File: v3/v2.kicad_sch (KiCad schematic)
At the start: 112 parts, among them J2 Conn_01x04_Pin, J3 Conn_01x04_Pin, SW1 SW_Push, SW10 SW_Push, SW11 SW_Push, SW12 SW_Push, SW13 SW_Push, SW14 SW_Push, SW15 SW_Push, SW16 SW_Push, SW17 SW_Push, SW18 SW_Push, SW19 SW_Push, SW2 SW_Push, SW20 SW_Push, SW21 SW_Push, SW22 SW_Push, SW23 SW_Push, SW24 SW_Push, SW25 SW_Push, SW26 SW_Push, SW27 SW_Push, SW28 SW_Push, SW29 SW_Push, SW3 SW_Push, SW30 SW_Push, SW31 SW_Push, SW32 SW_Push, SW33 RotaryEncoder_Switch, SW4 SW_Push, SW5 SW_Push, SW6 SW_Push, SW7 SW_Push, SW8 SW_Push, SW9 SW_Push, U1 Pico, U2 Pico

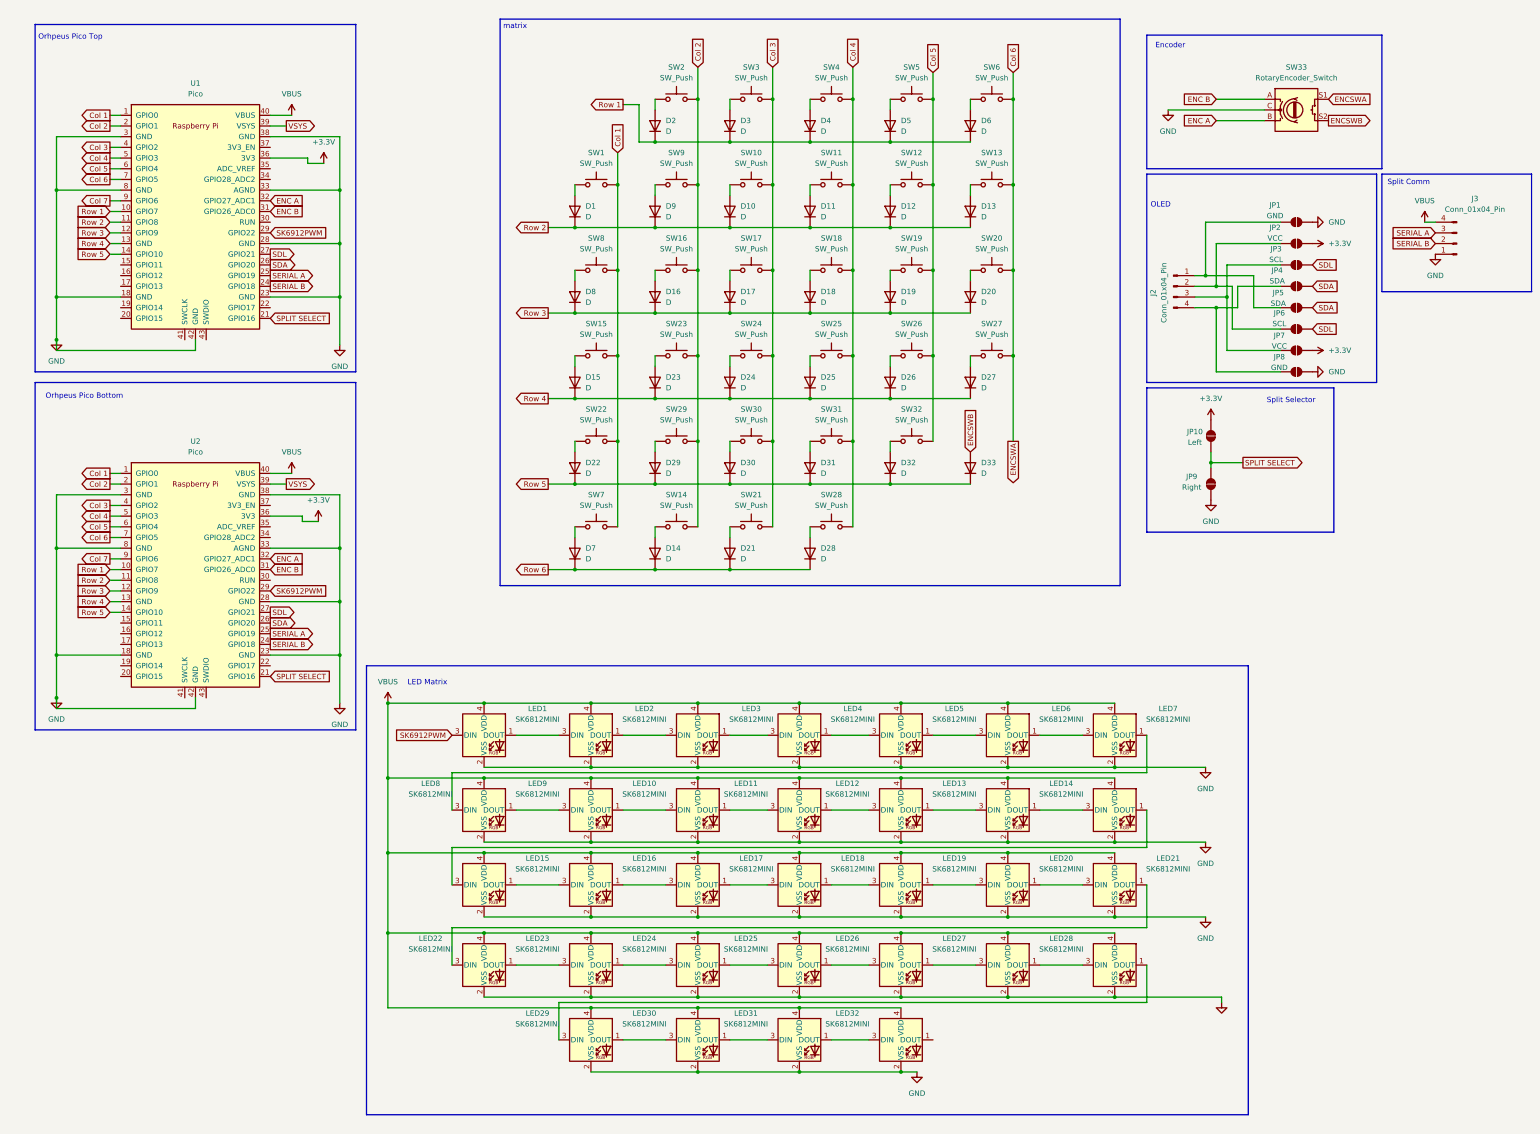
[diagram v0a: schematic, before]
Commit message: redid footprints and layout for pcb
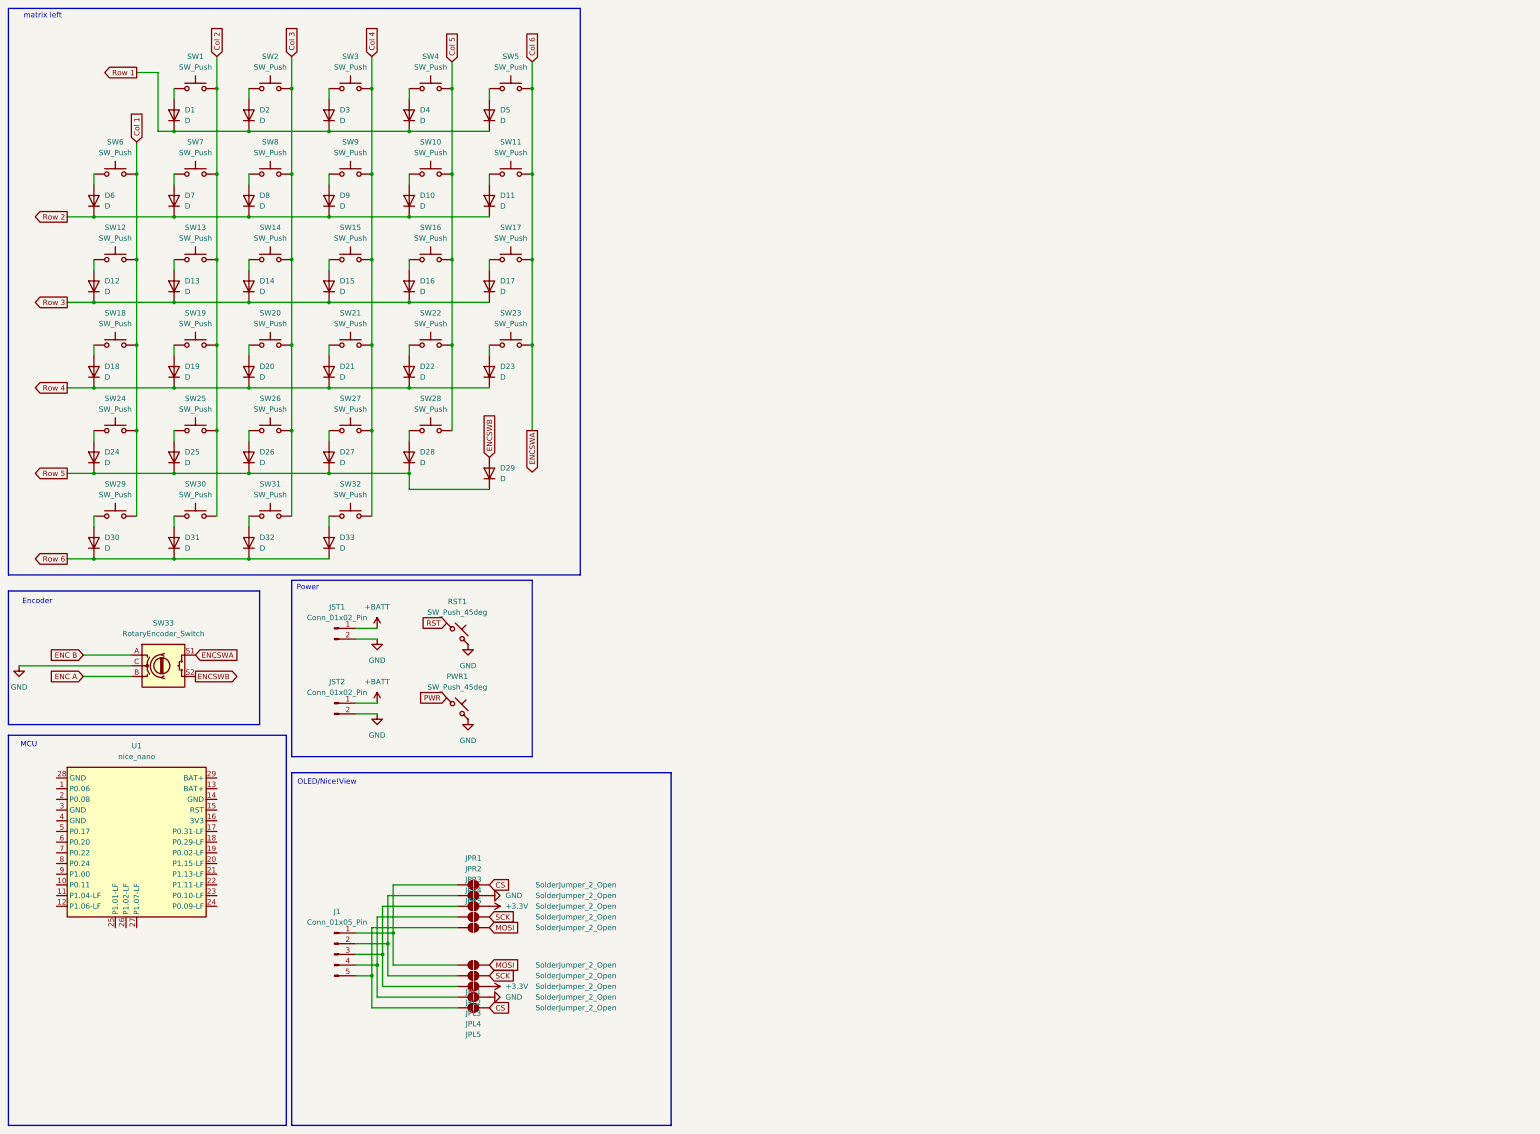
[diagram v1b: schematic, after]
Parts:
- removed J2: Conn_01x04_Pin, Keebio-Parts:I2C_Breakout, symbol Connector:Conn_01x04_Pin
- removed J3: Conn_01x04_Pin, Keebio-Parts:TRRS-PJ-320A-dual, symbol Connector:Conn_01x04_Pin
- removed JP1, JP8: GND, Jumper:SolderJumper-2_P1.3mm_Open_RoundedPad1.0x1.5mm, symbol Jumper:SolderJumper_2_Open
- removed JP10: Left, Jumper:SolderJumper-2_P1.3mm_Open_RoundedPad1.0x1.5mm, symbol Jumper:SolderJumper_2_Open
- removed JP2, JP7: VCC, Jumper:SolderJumper-2_P1.3mm_Open_RoundedPad1.0x1.5mm, symbol Jumper:SolderJumper_2_Open
- removed JP3, JP6: SCL, Jumper:SolderJumper-2_P1.3mm_Open_RoundedPad1.0x1.5mm, symbol Jumper:SolderJumper_2_Open
- removed JP4, JP5: SDA, Jumper:SolderJumper-2_P1.3mm_Open_RoundedPad1.0x1.5mm, symbol Jumper:SolderJumper_2_Open
- removed JP9: Right, Jumper:SolderJumper-2_P1.3mm_Open_RoundedPad1.0x1.5mm, symbol Jumper:SolderJumper_2_Open
- removed LED1, LED10, LED11, LED12, LED13, LED14, LED15, LED16, LED17, LED18, LED19, LED2, LED20, LED21, LED22, LED23, LED24, LED25, LED26, LED27, LED28, LED29, LED3, LED30, LED31, LED32, LED4, LED5, LED6, LED7, LED8, LED9: SK6812MINI, reversible-kicad-footprints:MX-1U-SK6812Mini-E, symbol LED:SK6812MINI
- removed U1, U2: Pico, Module:RaspberryPi_Pico_SMD_HandSolder, symbol RPi_Pico:Pico
- added J1: Conn_01x05_Pin, Connector_PinHeader_1.00mm:PinHeader_1x05_P1.00mm_Vertical, symbol Connector:Conn_01x05_Pin
- added JPL1, JPL2, JPL3, JPL4, JPL5, JPR1, JPR2, JPR3, JPR4, JPR5: SolderJumper_2_Open, Jumper:SolderJumper-2_P1.3mm_Open_RoundedPad1.0x1.5mm, symbol Jumper:SolderJumper_2_Open
- added JST1, JST2: Conn_01x02_Pin, Connector_JST:JST_PH_S2B-PH-K_1x02_P2.00mm_Horizontal, symbol Connector:Conn_01x02_Pin
- added PWR1, RST1: SW_Push_45deg, reversible-kicad-footprints:SMD_Push, symbol Switch:SW_Push_45deg
- added U1: nice_nano, PCM_marbastlib-xp-promicroish:nice_nano_AH_USBup, symbol PCM_marbastlib-promicroish:nice_nano
- D1: renamed from D2; footprint Keebio-Parts:Diode-Hybrid-Dual -> footprints:Diode-dual
- D10: renamed from D12; footprint Keebio-Parts:Diode-Hybrid-Dual -> footprints:Diode-dual
- D11: renamed from D13; footprint Keebio-Parts:Diode-Hybrid-Dual -> footprints:Diode-dual
- D12: renamed from D8; footprint Keebio-Parts:Diode-Hybrid-Dual -> footprints:Diode-dual
- D13: renamed from D16; footprint Keebio-Parts:Diode-Hybrid-Dual -> footprints:Diode-dual
- D14: renamed from D17; footprint Keebio-Parts:Diode-Hybrid-Dual -> footprints:Diode-dual
- D15: renamed from D18; footprint Keebio-Parts:Diode-Hybrid-Dual -> footprints:Diode-dual
- D16: renamed from D19; footprint Keebio-Parts:Diode-Hybrid-Dual -> footprints:Diode-dual
- D17: renamed from D20; footprint Keebio-Parts:Diode-Hybrid-Dual -> footprints:Diode-dual
- D18: renamed from D15; footprint Keebio-Parts:Diode-Hybrid-Dual -> footprints:Diode-dual
- D19: renamed from D23; footprint Keebio-Parts:Diode-Hybrid-Dual -> footprints:Diode-dual
- D2: renamed from D3; footprint Keebio-Parts:Diode-Hybrid-Dual -> footprints:Diode-dual
- D20: renamed from D24; footprint Keebio-Parts:Diode-Hybrid-Dual -> footprints:Diode-dual
- D21: renamed from D25; footprint Keebio-Parts:Diode-Hybrid-Dual -> footprints:Diode-dual
- D22: renamed from D26; footprint Keebio-Parts:Diode-Hybrid-Dual -> footprints:Diode-dual
- D23: renamed from D27; footprint Keebio-Parts:Diode-Hybrid-Dual -> footprints:Diode-dual
- D24: renamed from D22; footprint Keebio-Parts:Diode-Hybrid-Dual -> footprints:Diode-dual
- D25: renamed from D29; footprint Keebio-Parts:Diode-Hybrid-Dual -> footprints:Diode-dual
- D26: renamed from D30; footprint Keebio-Parts:Diode-Hybrid-Dual -> footprints:Diode-dual
- D27: renamed from D31; footprint Keebio-Parts:Diode-Hybrid-Dual -> footprints:Diode-dual
- D28: renamed from D32; footprint Keebio-Parts:Diode-Hybrid-Dual -> footprints:Diode-dual
- D29: renamed from D33; footprint Keebio-Parts:Diode-Hybrid-Dual -> footprints:Diode-dual
- D3: renamed from D4; footprint Keebio-Parts:Diode-Hybrid-Dual -> footprints:Diode-dual
- D30: renamed from D7; footprint Keebio-Parts:Diode-Hybrid-Dual -> footprints:Diode-dual
- D31: renamed from D14; footprint Keebio-Parts:Diode-Hybrid-Dual -> footprints:Diode-dual
- D32: renamed from D21; footprint Keebio-Parts:Diode-Hybrid-Dual -> footprints:Diode-dual
- D33: renamed from D28; footprint Keebio-Parts:Diode-Hybrid-Dual -> footprints:Diode-dual
- D4: renamed from D5; footprint Keebio-Parts:Diode-Hybrid-Dual -> footprints:Diode-dual
- D5: renamed from D6; footprint Keebio-Parts:Diode-Hybrid-Dual -> footprints:Diode-dual
- D6: renamed from D1; footprint Keebio-Parts:Diode-Hybrid-Dual -> footprints:Diode-dual
- D7: renamed from D9; footprint Keebio-Parts:Diode-Hybrid-Dual -> footprints:Diode-dual
- D8: renamed from D10; footprint Keebio-Parts:Diode-Hybrid-Dual -> footprints:Diode-dual
- D9: renamed from D11; footprint Keebio-Parts:Diode-Hybrid-Dual -> footprints:Diode-dual
- SW1: renamed from SW2; footprint reversible-kicad-footprints:MX-1U-Hotswap -> footprints:gateron-ks27-hotswap-reversible
- SW10: renamed from SW12; footprint reversible-kicad-footprints:MX-1U-Hotswap -> footprints:gateron-ks27-hotswap-reversible
- SW11: renamed from SW13; footprint reversible-kicad-footprints:MX-1U-Hotswap -> footprints:gateron-ks27-hotswap-reversible
- SW12: renamed from SW8; footprint reversible-kicad-footprints:MX-1U-Hotswap -> footprints:gateron-ks27-hotswap-reversible
- SW13: renamed from SW16; footprint reversible-kicad-footprints:MX-1U-Hotswap -> footprints:gateron-ks27-hotswap-reversible
- SW14: renamed from SW17; footprint reversible-kicad-footprints:MX-1U-Hotswap -> footprints:gateron-ks27-hotswap-reversible
- SW15: renamed from SW18; footprint reversible-kicad-footprints:MX-1U-Hotswap -> footprints:gateron-ks27-hotswap-reversible
- SW16: renamed from SW19; footprint reversible-kicad-footprints:MX-1U-Hotswap -> footprints:gateron-ks27-hotswap-reversible
- SW17: renamed from SW20; footprint reversible-kicad-footprints:MX-1U-Hotswap -> footprints:gateron-ks27-hotswap-reversible
- SW18: renamed from SW15; footprint reversible-kicad-footprints:MX-1U-Hotswap -> footprints:gateron-ks27-hotswap-reversible
- SW19: renamed from SW23; footprint reversible-kicad-footprints:MX-1U-Hotswap -> footprints:gateron-ks27-hotswap-reversible
- SW2: renamed from SW3; footprint reversible-kicad-footprints:MX-1U-Hotswap -> footprints:gateron-ks27-hotswap-reversible
- SW20: renamed from SW24; footprint reversible-kicad-footprints:MX-1U-Hotswap -> footprints:gateron-ks27-hotswap-reversible
- SW21: renamed from SW25; footprint reversible-kicad-footprints:MX-1U-Hotswap -> footprints:gateron-ks27-hotswap-reversible
- SW22: renamed from SW26; footprint reversible-kicad-footprints:MX-1U-Hotswap -> footprints:gateron-ks27-hotswap-reversible
- SW23: renamed from SW27; footprint reversible-kicad-footprints:MX-1U-Hotswap -> footprints:gateron-ks27-hotswap-reversible
- SW24: renamed from SW22; footprint reversible-kicad-footprints:MX-1U-Hotswap -> footprints:gateron-ks27-hotswap-reversible
- SW25: renamed from SW29; footprint reversible-kicad-footprints:MX-1U-Hotswap -> footprints:gateron-ks27-hotswap-reversible
- SW26: renamed from SW30; footprint reversible-kicad-footprints:MX-1U-Hotswap -> footprints:gateron-ks27-hotswap-reversible
- SW27: renamed from SW31; footprint reversible-kicad-footprints:MX-1U-Hotswap -> footprints:gateron-ks27-hotswap-reversible
- SW28: renamed from SW32; footprint reversible-kicad-footprints:MX-1U-Hotswap -> footprints:gateron-ks27-hotswap-reversible
- SW29: renamed from SW7; footprint reversible-kicad-footprints:MX-1U-Hotswap -> footprints:gateron-ks27-hotswap-reversible
- SW3: renamed from SW4; footprint reversible-kicad-footprints:MX-1U-Hotswap -> footprints:gateron-ks27-hotswap-reversible
- SW30: renamed from SW14; footprint reversible-kicad-footprints:MX-1U-Hotswap -> footprints:gateron-ks27-hotswap-reversible
- SW31: renamed from SW21; footprint reversible-kicad-footprints:MX-1U-Hotswap -> footprints:gateron-ks27-hotswap-reversible
- SW32: renamed from SW28; footprint reversible-kicad-footprints:MX-1U-Hotswap -> footprints:gateron-ks27-hotswap-reversible
- SW33: footprint Keebio-Parts:RotaryEncoder_EC11 -> Keebio-Parts.pretty-master:RotaryEncoder_EC11
- SW4: renamed from SW5; footprint reversible-kicad-footprints:MX-1U-Hotswap -> footprints:gateron-ks27-hotswap-reversible
- SW5: renamed from SW6; footprint reversible-kicad-footprints:MX-1U-Hotswap -> footprints:gateron-ks27-hotswap-reversible
- SW6: renamed from SW1; footprint reversible-kicad-footprints:MX-1U-Hotswap -> footprints:gateron-ks27-hotswap-reversible
- SW7: renamed from SW9; footprint reversible-kicad-footprints:MX-1U-Hotswap -> footprints:gateron-ks27-hotswap-reversible
- SW8: renamed from SW10; footprint reversible-kicad-footprints:MX-1U-Hotswap -> footprints:gateron-ks27-hotswap-reversible
- SW9: renamed from SW11; footprint reversible-kicad-footprints:MX-1U-Hotswap -> footprints:gateron-ks27-hotswap-reversible
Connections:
- net +3.3V: now also JPL3.2 (B), JPR3.2 (B)
- net GND: now also JPL4.2 (B), JPR2.2 (B), JST1.2 (Pin_2), JST2.2 (Pin_2), PWR1.2, RST1.2
- new net: J1.5 (Pin_5), JPL5.1 (A), JPR5.1 (A)
- new net: J1.1 (Pin_1), JPL1.1 (A), JPR1.1 (A)
- new net: J1.2 (Pin_2), JPL2.1 (A), JPR2.1 (A)
- new net: J1.3 (Pin_3), JPL3.1 (A), JPR3.1 (A)
- new net: J1.4 (Pin_4), JPL4.1 (A), JPR4.1 (A)
- new net +BATT: JST1.1 (Pin_1), JST2.1 (Pin_1)
- new net CS: JPL5.2 (B), JPR1.2 (B)
- new net MOSI: JPL1.2 (B), JPR5.2 (B)
- new net PWR: PWR1.1
- new net RST: RST1.1
- new net SCK: JPL2.2 (B), JPR4.2 (B)
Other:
- note added: "MCU"
- note added: "OLED/Nice!View"
- note added: "Power"
- note added: "matrix left"
- note removed: "LED Matrix"
- note removed: "OLED"
- note removed: "Orhpeus Pico Bottom"
- note removed: "Orhpeus Pico Top"
- note removed: "Split Comm"
- note removed: "Split Selector"
- note removed: "matrix"
- moved on the sheet: D1, D10, D11, D12, D13, D14, D15, D16, D17, D18, D19, D2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

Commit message: start placing switches
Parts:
- J1: footprint Connector_PinHeader_1.00mm:PinHeader_1x05_P1.00mm_Vertical -> Connector_PinHeader_2.54mm:PinHeader_1x05_P2.54mm_Vertical
- PWR1, RST1: footprint reversible-kicad-footprints:SMD_Push -> footprints:EVQ-P7C-Reversible
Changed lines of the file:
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@@
 			)
 		)
-		(property "Footprint" "Connector_PinHeader_1.00mm:PinHeader_1x05_P1.00mm_Vertical"
+		(property "Footprint" "Connector_PinHeader_2.54mm:PinHeader_1x05_P2.54mm_Vertical"
 			(at 95.25 241.3 0)
 			(effects
@@
 			)
 		)
-		(property "Footprint" "reversible-kicad-footprints:SMD_Push"
+		(property "Footprint" "footprints:EVQ-P7C-Reversible"
 			(at 124.46 165.1 0)
 			(effects
@@
 			)
 		)
-		(property "Footprint" "reversible-kicad-footprints:SMD_Push"
+		(property "Footprint" "footprints:EVQ-P7C-Reversible"
 			(at 124.46 182.88 0)
 			(effects

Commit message: added all needed labels
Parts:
- added U2: nice_nano_right, PCM_marbastlib-xp-promicroish:nice_nano_AH_USBup, symbol PCM_marbastlib-promicroish:nice_nano
- U1: value nice_nano -> nice_nano_left
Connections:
- net +3.3V: now also U1.16 (3V3), U2.16 (3V3)
- net +BATT: now also U1.13 (BAT+), U1.29 (BAT+), U2.13 (BAT+), U2.29 (BAT+)
- net CS: now also U1.1 (P0.06), U2.1 (P0.06)
- net Col 1: now also U1.2 (P0.08), U2.2 (P0.08)
- net Col 2: now also U1.7 (P0.22), U2.7 (P0.22)
- net Col 3: now also U1.8 (P0.24), U2.8 (P0.24)
- net Col 4: now also U1.9 (P1.00), U2.9 (P1.00)
- net Col 5: now also U1.10 (P0.11), U2.10 (P0.11)
- net Col 6: now also U1.11 (P1.04-LF), U2.11 (P1.04-LF)
- net ENC A: now also U1.12 (P1.06-LF), U2.12 (P1.06-LF)
- net ENC B: now also U1.23 (P0.10-LF), U2.23 (P0.10-LF)
- net GND: now also U1.14 (GND), U1.28 (GND), U1.3 (GND), U1.4 (GND), U2.14 (GND), U2.28 (GND), U2.3 (GND), U2.4 (GND)
- net MOSI: now also U1.6 (P0.20), U2.6 (P0.20)
- net PWR: now also U1.24 (P0.09-LF), U2.24 (P0.09-LF)
- net RST: now also U1.15 (RST), U2.15 (RST)
- net Row 1: now also U1.17 (P0.31-LF), U2.17 (P0.31-LF)
- net Row 2: now also U1.18 (P0.29-LF), U2.18 (P0.29-LF)
- net Row 3: now also U1.19 (P0.02-LF), U2.19 (P0.02-LF)
- net Row 4: now also U1.20 (P1.15-LF), U2.20 (P1.15-LF)
- net Row 5: now also U1.21 (P1.13-LF), U2.21 (P1.13-LF)
- net Row 6: now also U1.22 (P1.11-LF), U2.22 (P1.11-LF)
- net SCK: now also U1.5 (P0.17), U2.5 (P0.17)

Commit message: reversible nice!nano
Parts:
- removed U2: nice_nano_right, PCM_marbastlib-xp-promicroish:nice_nano_AH_USBup, symbol PCM_marbastlib-promicroish:nice_nano
- U1: footprint PCM_marbastlib-xp-promicroish:nice_nano_AH_USBup -> PCM_marbastlib-xp-promicroish:nice_nano_AH_Reversible
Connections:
- no-connect marks 0 -> 3
